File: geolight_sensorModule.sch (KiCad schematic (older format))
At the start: 20 parts, among them IC1 ATTINY841-SSU, P1 5V, P2 ICSP, P3 IN, P4 OUT, P5 OUT (JP for IN), P6 UART(test), U1 TCRT5000/L, Y1 16Mhz

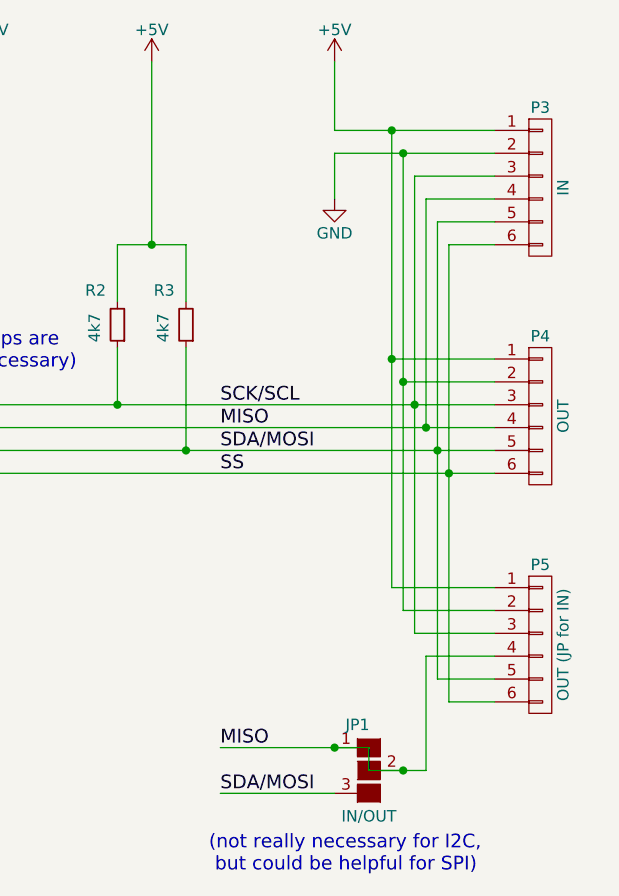
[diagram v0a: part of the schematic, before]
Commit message: removed 3rd, reversible jumper connector (difficult to mirror if reversible, probably not necessary to have 3)
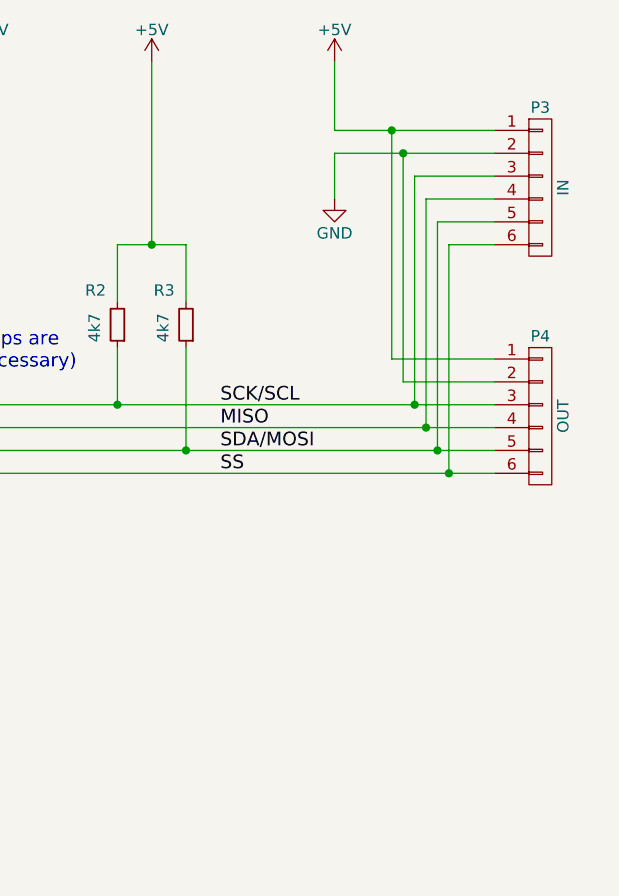
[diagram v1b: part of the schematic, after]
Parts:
- removed JP1: IN/OUT, Connect:GS3, symbol GS3
- removed P5: OUT (JP for IN), Pin_Headers:Pin_Header_Angled_1x06, symbol CONN_01X06
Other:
- note removed: "(not really necessary for I2C, \n but could be helpful for SPI)"
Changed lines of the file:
@@
-$EndComp
-$Comp
-L CONN_01X06 P5
-U 1 1 57CBE4B3
-P 9550 4850
-F 0 "P5" H 9550 5200 50  0000 C CNN
-F 1 "OUT (JP for IN)" V 9650 4850 50  0000 C CNN
-F 2 "Pin_Headers:Pin_Header_Angled_1x06" H 9550 4850 50  0001 C CNN
-F 3 "" H 9550 4850 50  0000 C CNN
-	1    9550 4850
-	1    0    0    -1
 $EndComp
 $Comp
@@
 Text Label 8150 4100 0    60   ~ 0
 SS
-Text Label 8150 5300 0    60   ~ 0
-MISO
-Text Label 8150 5500 0    60   ~ 0
-SDA/MOSI
-$Comp
-L GS3 JP1
-U 1 1 57CC0AD0
-P 8800 5400
-F 0 "JP1" H 8750 5600 50  0000 C CNN
-F 1 "IN/OUT" H 8800 5200 50  0000 C CNN
-F 2 "Connect:GS3" V 8888 5326 50  0001 C CNN
-F 3 "" H 8800 5400 50  0000 C CNN
-	1    8800 5400
-	1    0    0    -1
-$EndComp
 $Comp
 L CONN_02X03 P2
@@
 	1    0    0    -1
 $EndComp
-Wire Wire Line
-	5250 4000 9350 4000
-Wire Wire Line
-	5250 3900 9350 3900
-Connection ~ 6300 2900
-Wire Wire Line
-	5850 2900 6750 2900
-Wire Wire Line
-	9100 5000 9350 5000
-Wire Wire Line
-	9100 3000 9100 5000
-Connection ~ 8900 2600
-Connection ~ 8900 3600
-Wire Wire Line
-	8900 3600 9350 3600
-Connection ~ 8950 3700
-Wire Wire Line
-	9350 3700 8950 3700
-Connection ~ 9000 3800
-Wire Wire Line
-	5250 3800 9350 3800
-Connection ~ 9050 3900
-Connection ~ 9100 4000
-Connection ~ 9150 4100
-Wire Wire Line
-	5250 4100 9350 4100
-Wire Wire Line
-	8900 4600 9350 4600
-Wire Wire Line
-	8650 2600 9350 2600
-Wire Wire Line
-	8900 2600 8900 4600
-Wire Wire Line
-	8950 4700 9350 4700
-Wire Wire Line
-	8650 2700 9350 2700
-Wire Wire Line
-	9000 4800 9350 4800
-Wire Wire Line
-	9000 2800 9000 4800
-Wire Wire Line
-	9350 2800 9000 2800
-Wire Wire Line
-	8800 5400 9050 5400
-Wire Wire Line
-	9350 2900 9050 2900
-Wire Wire Line
-	9100 3000 9350 3000
-Wire Wire Line
-	9150 5100 9350 5100
-Wire Wire Line
-	9150 3100 9150 5100
-Wire Wire Line
-	9350 3100 9150 3100
-Wire Wire Line
-	4300 2700 4300 2800
-Wire Wire Line
-	4300 2400 4300 2500
-Wire Wire Line
-	7150 2350 7150 2300
-Wire Wire Line
-	7000 2350 7150 2350
-Wire Wire Line
-	6700 2350 6800 2350
-Wire Wire Line
-	6750 2900 6750 2650
-Wire Wire Line
-	6750 2650 6700 2650
-Wire Wire Line
-	5850 2650 5850 2900
-Wire Wire Line
-	5900 2650 5850 2650
-Wire Wire Line
-	2500 4400 2500 4850
-Wire Wire Line
-	2750 4400 2500 4400
-Wire Wire Line
-	3150 4500 3000 4500
-Wire Wire Line
-	3150 4300 3000 4300
-Wire Wire Line
-	3450 2700 3450 2650
-Wire Wire Line
-	3650 2700 3450 2700
-Wire Wire Line
-	3450 2500 3450 2550
-Wire Wire Line
-	3650 2500 3450 2500
-Wire Wire Line
-	3650 2700 3650 2900
-Wire Wire Line
-	3650 2300 3650 2500
-Wire Wire Line
-	6250 4600 6250 4850
-Wire Wire Line
-	6100 4600 6250 4600
-Wire Wire Line
-	5700 4600 5900 4600
-Wire Wire Line
-	5250 4600 5500 4600
-Wire Wire Line
-	3150 4600 3100 4600
-Wire Wire Line
-	3100 4600 3100 4750
-Wire Wire Line
-	3050 3400 3150 3400
-Wire Wire Line
-	5250 3400 5700 3400
-Wire Wire Line
-	8150 5300 8800 5300
-Wire Wire Line
-	8650 5500 8150 5500
-Wire Wire Line
-	8800 5300 8800 5400
-Connection ~ 8950 5400
-Connection ~ 8650 5300
-Wire Wire Line
-	9050 2900 9050 3900
-Wire Wire Line
-	8950 2700 8950 4700
-Wire Wire Line
-	8650 2900 8650 2700
-Connection ~ 8950 2700
-Wire Wire Line
-	8650 2600 8650 2300
-Wire Wire Line
-	9350 4900 9050 4900
-Wire Wire Line
-	9050 4900 9050 5400
-Wire Wire Line
-	2050 2650 2650 2650
-Wire Wire Line
-	1550 2550 1050 2550
-Wire Wire Line
-	1550 2650 1050 2650
-Wire Wire Line
-	1550 2750 1050 2750
-Wire Wire Line
-	2050 2750 2150 2750
-Wire Wire Line
-	2150 2750 2150 2900
-Wire Wire Line
-	2050 2550 2150 2550
-Wire Wire Line
-	2150 2550 2150 2300
-Wire Wire Line
-	3150 4200 3050 4200
-Wire Wire Line
-	3050 4200 3050 3900
-Wire Wire Line
-	3050 2300 3050 3700
-Connection ~ 3050 3400
-Wire Wire Line
-	4700 2800 4700 2700
-Wire Wire Line
-	4700 2400 4700 2500
-Wire Wire Line
-	4300 2800 4700 2800
-Wire Wire Line
-	4500 2900 4500 2800
-Connection ~ 4500 2800
 $Comp
 L +5V #PWR013
@@
 	1    0    0    -1
 $EndComp
-Wire Wire Line
-	4300 2400 4700 2400
-Wire Wire Line
-	4500 2300 4500 2400
-Connection ~ 4500 2400
-Wire Wire Line
-	3100 4750 2500 4750
-Connection ~ 2500 4750
 $Comp
 L R_Small R2
@@
 	-1   0    0    1
 $EndComp
-Wire Wire Line
-	7700 3550 7700 3800
-Wire Wire Line
-	8000 3550 8000 4000
-Wire Wire Line
-	5700 3400 5700 2350
-Wire Wire Line
-	7700 3350 7700 3100
-Wire Wire Line
-	8000 3100 8000 3350
 $Comp
 L +5V #PWR014
@@
 	1    0    0    -1
 $EndComp
-Connection ~ 7850 3100
 Text Notes 6700 3650 0    60   ~ 0
 (these pullups are \n likely unnecessary)
-Wire Wire Line
-	5250 3500 5450 3500
-Wire Wire Line
-	5250 3600 5450 3600
-Wire Wire Line
-	7700 3100 8000 3100
-Wire Wire Line
-	7850 2300 7850 3100
-Wire Wire Line
-	5550 2350 5900 2350
-Connection ~ 7700 3800
-Connection ~ 8000 4000
-Text Notes 8100 5850 0    60   ~ 0
-(not really necessary for I2C, \n but could be helpful for SPI)
 $Comp
 L CONN_01X02 P6
@@
 $EndComp
 Wire Wire Line
+	5250 4000 9350 4000
+Wire Wire Line
+	5250 3900 9350 3900
+Connection ~ 6300 2900
+Wire Wire Line
+	5850 2900 6750 2900
+Connection ~ 8900 2600
+Wire Wire Line
+	8900 3600 9350 3600
+Wire Wire Line
+	9350 3700 8950 3700
+Connection ~ 9000 3800
+Wire Wire Line
+	5250 3800 9350 3800
+Connection ~ 9050 3900
+Connection ~ 9100 4000
+Connection ~ 9150 4100
+Wire Wire Line
+	5250 4100 9350 4100
+Wire Wire Line
+	8650 2600 9350 2600
+Wire Wire Line
+	8650 2700 9350 2700
+Wire Wire Line
+	9350 2800 9000 2800
+Wire Wire Line
+	9350 2900 9050 2900
+Wire Wire Line
+	9100 3000 9350 3000
+Wire Wire Line
+	9350 3100 9150 3100
+Wire Wire Line
+	4300 2700 4300 2800
+Wire Wire Line
+	4300 2400 4300 2500
+Wire Wire Line
+	7150 2350 7150 2300
+Wire Wire Line
+	7000 2350 7150 2350
+Wire Wire Line
+	6700 2350 6800 2350
+Wire Wire Line
+	6750 2900 6750 2650
+Wire Wire Line
+	6750 2650 6700 2650
+Wire Wire Line
+	5850 2650 5850 2900
+Wire Wire Line
+	5900 2650 5850 2650
+Wire Wire Line
+	2500 4400 2500 4850
+Wire Wire Line
+	2750 4400 2500 4400
+Wire Wire Line
+	3150 4500 3000 4500
+Wire Wire Line
+	3150 4300 3000 4300
+Wire Wire Line
+	3450 2700 3450 2650
+Wire Wire Line
+	3650 2700 3450 2700
+Wire Wire Line
+	3450 2500 3450 2550
+Wire Wire Line
+	3650 2500 3450 2500
+Wire Wire Line
+	3650 2700 3650 2900
+Wire Wire Line
+	3650 2300 3650 2500
+Wire Wire Line
+	6250 4600 6250 4850
+Wire Wire Line
+	6100 4600 6250 4600
+Wire Wire Line
+	5700 4600 5900 4600
+Wire Wire Line
+	5250 4600 5500 4600
+Wire Wire Line
+	3150 4600 3100 4600
+Wire Wire Line
+	3100 4600 3100 4750
+Wire Wire Line
+	3050 3400 3150 3400
+Wire Wire Line
+	5250 3400 5700 3400
+Wire Wire Line
+	9050 2900 9050 3900
+Wire Wire Line
+	8650 2900 8650 2700
+Connection ~ 8950 2700
+Wire Wire Line
+	8650 2600 8650 2300
+Wire Wire Line
+	2050 2650 2650 2650
+Wire Wire Line
+	1550 2550 1050 2550
+Wire Wire Line
+	1550 2650 1050 2650
+Wire Wire Line
+	1550 2750 1050 2750
+Wire Wire Line
+	2050 2750 2150 2750
+Wire Wire Line
+	2150 2750 2150 2900
+Wire Wire Line
+	2050 2550 2150 2550
+Wire Wire Line
+	2150 2550 2150 2300
+Wire Wire Line
+	3150 4200 3050 4200
+Wire Wire Line
+	3050 4200 3050 3900
+Wire Wire Line
+	3050 2300 3050 3700
+Connection ~ 3050 3400
+Wire Wire Line
+	4700 2800 4700 2700
+Wire Wire Line
+	4700 2400 4700 2500
+Wire Wire Line
+	4300 2800 4700 2800
+Wire Wire Line
+	4500 2900 4500 2800
+Connection ~ 4500 2800
+Wire Wire Line
+	4300 2400 4700 2400
+Wire Wire Line
+	4500 2300 4500 2400
+Connection ~ 4500 2400
+Wire Wire Line
+	3100 4750 2500 4750
+Connection ~ 2500 4750
+Wire Wire Line
+	7700 3550 7700 3800
+Wire Wire Line
+	8000 3550 8000 4000
+Wire Wire Line
+	5700 3400 5700 2350
+Wire Wire Line
+	7700 3350 7700 3100
+Wire Wire Line
+	8000 3100 8000 3350
+Connection ~ 7850 3100
+Wire Wire Line
+	5250 3500 5450 3500
+Wire Wire Line
+	5250 3600 5450 3600
+Wire Wire Line
+	7700 3100 8000 3100
+Wire Wire Line
+	7850 2300 7850 3100
+Wire Wire Line
+	5550 2350 5900 2350
+Connection ~ 7700 3800
+Connection ~ 8000 4000
+Wire Wire Line
 	5200 2300 5200 2350
 Wire Wire Line
 	5200 2350 5350 2350
 Connection ~ 5700 2350
+Wire Wire Line
+	9150 3100 9150 4100
+Wire Wire Line
+	9100 3000 9100 4000
+Wire Wire Line
+	9000 2800 9000 3800
+Wire Wire Line
+	8950 3700 8950 2700
+Wire Wire Line
+	8900 2600 8900 3600
 $EndSCHEMATC

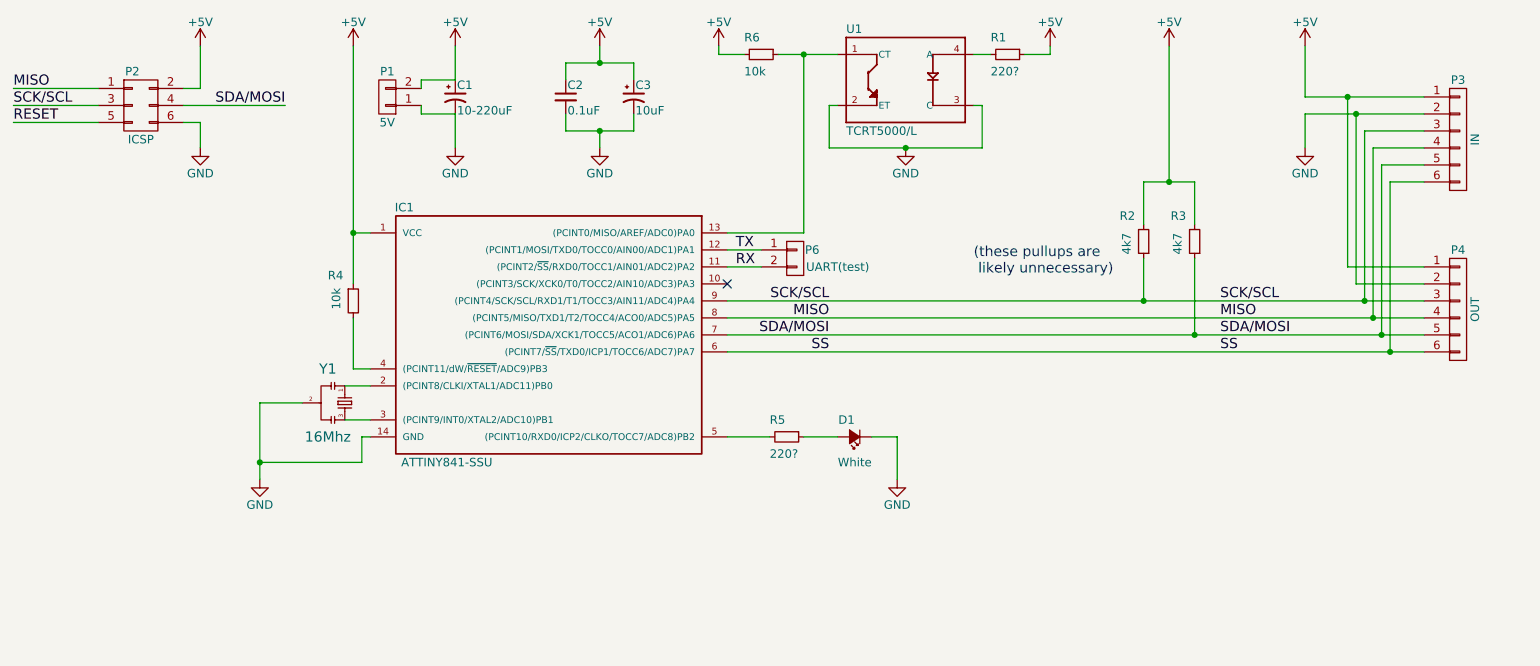
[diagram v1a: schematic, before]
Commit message: clean up schematic. Add SPI/I2C jumper.
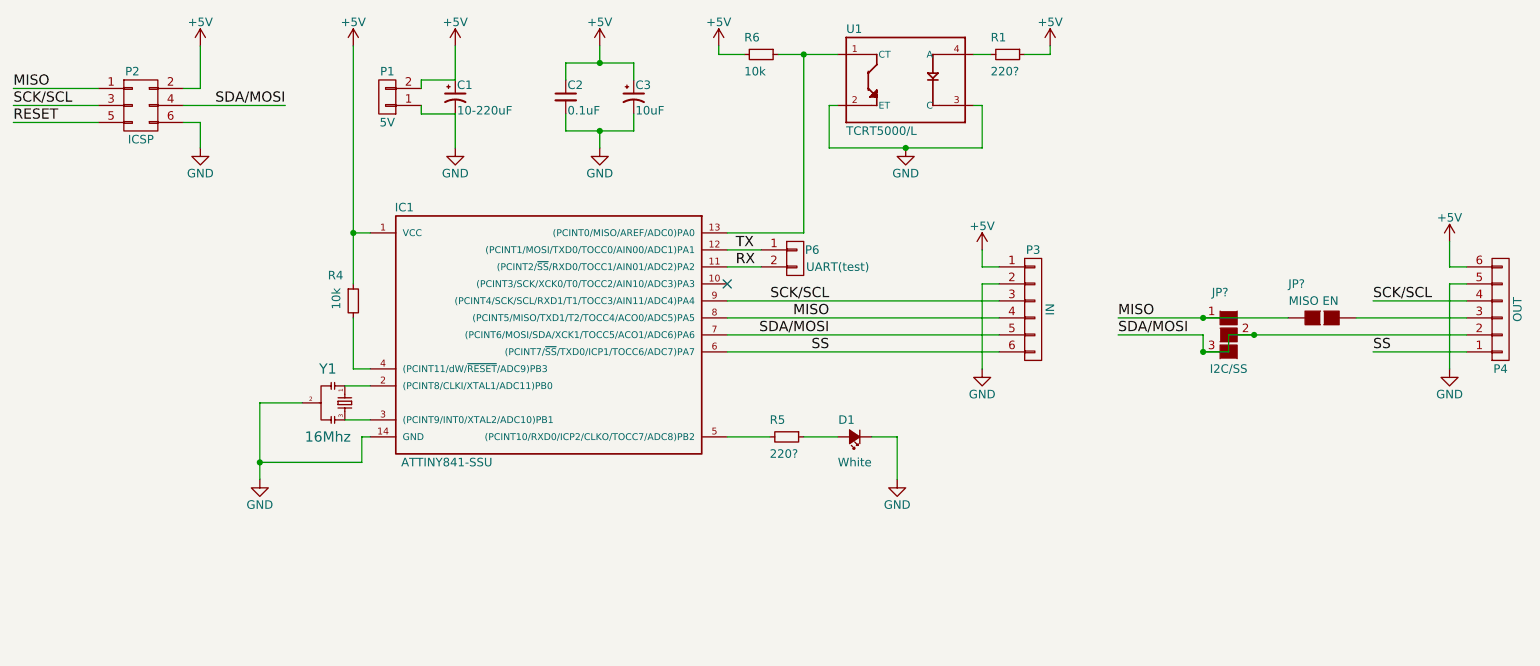
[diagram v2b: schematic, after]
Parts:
- removed R2, R3: 4k7, Discret:R1, symbol R_Small
- added JP?: I2C/SS, GS3, symbol GS3
- added JP?: MISO EN, GS2, symbol GS2
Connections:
- net +5V: now also P4.6 (P6); no longer P4.1 (P1)
- net GND: now also P4.5 (P5); no longer P4.2 (P2)
- net MISO: now also JP?.1 (G1), JP?.2 (G2); no longer P4.4 (P4)
- net SCK/SCL: now also P4.4 (P4); no longer P4.3 (P3)
- net SDA/MOSI: now also P4.2 (P2), JP?.2 (G2), JP?.3 (G3); no longer P4.5 (P5)
- net SS: now also P4.1 (P1); no longer P4.6 (P6)
- new net: JP?.1 (G1), P4.3 (P3)
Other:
- note removed: "(these pullups are \n likely unnecessary)"
- moved on the sheet: P3, P4

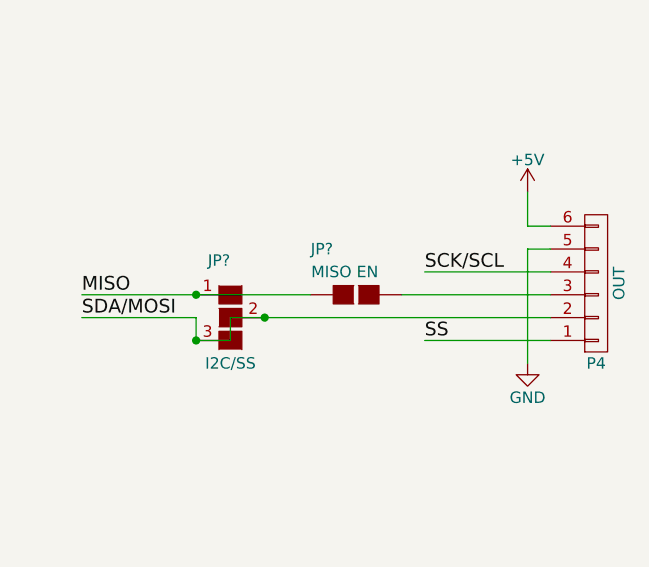
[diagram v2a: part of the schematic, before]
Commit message: fixed mirrored in/out. updated netlist, footprints, PCB. Fixed UART test point rats nest
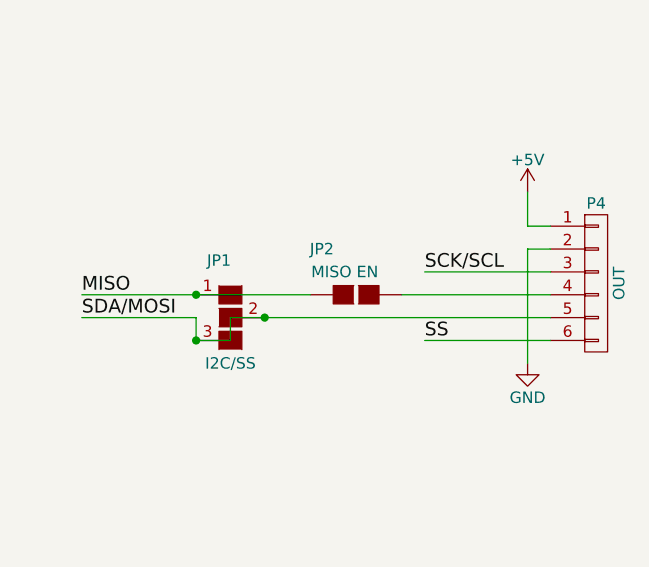
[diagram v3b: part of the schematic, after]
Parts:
- JP1: renamed from JP?; footprint GS3 -> Connect:GS3
- JP2: renamed from JP?; footprint GS2 -> Connect:GS2
- P3, P4: footprint Pin_Headers:Pin_Header_Angled_1x06 -> Pin_Headers:Pin_Header_Straight_1x06
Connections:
- net +5V: now also P4.1 (P1); no longer P4.6 (P6)
- net GND: now also P4.2 (P2); no longer P4.5 (P5)
- net SCK/SCL: now also P4.3 (P3); no longer P4.4 (P4)
- net SDA/MOSI: now also P4.5 (P5); no longer P4.2 (P2)
- net SS: now also P4.6 (P6); no longer P4.1 (P1)
- net at JP2.1 (G1): now also P4.4 (P4); no longer P4.3 (P3)
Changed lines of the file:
@@
 F 0 "P3" H 7050 4200 50  0000 C CNN
 F 1 "IN" V 7150 3850 50  0000 C CNN
-F 2 "Pin_Headers:Pin_Header_Angled_1x06" H 7050 3850 50  0001 C CNN
+F 2 "Pin_Headers:Pin_Header_Straight_1x06" H 7050 3850 50  0001 C CNN
 F 3 "" H 7050 3850 50  0000 C CNN
 	1    7050 3850
@@
 F 0 "P4" H 9800 4200 50  0000 C CNN
 F 1 "OUT" V 9900 3850 50  0000 C CNN
-F 2 "Pin_Headers:Pin_Header_Angled_1x06" H 9800 3850 50  0001 C CNN
+F 2 "Pin_Headers:Pin_Header_Straight_1x06" H 9800 3850 50  0001 C CNN
 F 3 "" H 9800 3850 50  0000 C CNN
 	1    9800 3850
-	1    0    0    1
+	1    0    0    -1
 $EndComp
 $Comp
@@
 SDA/MOSI
 $Comp
-L GND #PWR010
+L GND #PWR09
 U 1 1 57CC2E31
 P 2150 2900
-F 0 "#PWR010" H 2150 2650 50  0001 C CNN
+F 0 "#PWR09" H 2150 2650 50  0001 C CNN
 F 1 "GND" H 2150 2750 50  0000 C CNN
 F 2 "" H 2150 2900 50  0000 C CNN
@@
 $EndComp
 $Comp
-L +5V #PWR011
+L +5V #PWR010
 U 1 1 57CC2EE1
 P 2150 2300
-F 0 "#PWR011" H 2150 2150 50  0001 C CNN
+F 0 "#PWR010" H 2150 2150 50  0001 C CNN
 F 1 "+5V" H 2150 2440 50  0000 C CNN
 F 2 "" H 2150 2300 50  0000 C CNN
@@
 $EndComp
 $Comp
-L GND #PWR012
+L GND #PWR011
 U 1 1 57CC3ABE
 P 4500 2900
-F 0 "#PWR012" H 4500 2650 50  0001 C CNN
+F 0 "#PWR011" H 4500 2650 50  0001 C CNN
 F 1 "GND" H 4500 2750 50  0000 C CNN
 F 2 "" H 4500 2900 50  0000 C CNN
@@
 $EndComp
 $Comp
-L +5V #PWR013
+L +5V #PWR012
 U 1 1 57CC3AB8
 P 4500 2300
-F 0 "#PWR013" H 4500 2150 50  0001 C CNN
+F 0 "#PWR012" H 4500 2150 50  0001 C CNN
 F 1 "+5V" H 4500 2440 50  0000 C CNN
 F 2 "" H 4500 2300 50  0000 C CNN
@@
 $EndComp
 $Comp
-L +5V #PWR015
+L +5V #PWR013
 U 1 1 57CBD563
 P 5200 2300
-F 0 "#PWR015" H 5200 2150 50  0001 C CNN
+F 0 "#PWR013" H 5200 2150 50  0001 C CNN
 F 1 "+5V" H 5200 2440 50  0000 C CNN
 F 2 "" H 5200 2300 50  0000 C CNN
@@
 $EndComp
 $Comp
-L +5V #PWR?
+L +5V #PWR014
 U 1 1 57CBF61D
 P 9500 3450
-F 0 "#PWR?" H 9500 3300 50  0001 C CNN
+F 0 "#PWR014" H 9500 3300 50  0001 C CNN
 F 1 "+5V" H 9500 3590 50  0000 C CNN
 F 2 "" H 9500 3450 50  0000 C CNN
@@
 $EndComp
 $Comp
-L GND #PWR?
+L GND #PWR015
 U 1 1 57CBF758
 P 9500 4200
-F 0 "#PWR?" H 9500 3950 50  0001 C CNN
+F 0 "#PWR015" H 9500 3950 50  0001 C CNN
 F 1 "GND" H 9500 4050 50  0000 C CNN
 F 2 "" H 9500 4200 50  0000 C CNN
@@
 	8050 4100 8200 4100
 $Comp
-L GS3 JP?
+L GS3 JP1
 U 1 1 57CC065C
 P 8200 4000
-F 0 "JP?" H 8150 4250 50  0000 C CNN
+F 0 "JP1" H 8150 4250 50  0000 C CNN
 F 1 "I2C/SS" H 8200 3800 50  0000 C CNN
-F 2 "GS3" V 8288 3926 50  0001 C CNN
+F 2 "Connect:GS3" V 8288 3926 50  0001 C CNN
 F 3 "" H 8200 4000 50  0000 C CNN
 	1    8200 4000
@@
 	6750 3600 6850 3600
 $Comp
-L GND #PWR?
+L GND #PWR016
 U 1 1 57CC13DF
 P 6750 4200
-F 0 "#PWR?" H 6750 3950 50  0001 C CNN
+F 0 "#PWR016" H 6750 3950 50  0001 C CNN
 F 1 "GND" H 6750 4050 50  0000 C CNN
 F 2 "" H 6750 4200 50  0000 C CNN
@@
 	9500 3600 9600 3600
 $Comp
-L GS2 JP?
+L GS2 JP2
 U 1 1 57CC1D1D
 P 8750 3900
-F 0 "JP?" V 8550 3750 50  0000 C CNN
+F 0 "JP2" V 8550 3750 50  0000 C CNN
 F 1 "MISO EN" V 8650 3850 50  0000 C CNN
-F 2 "GS2" V 8824 3900 50  0001 C CNN
+F 2 "Connect:GS2" V 8824 3900 50  0001 C CNN
 F 3 "" H 8750 3900 50  0000 C CNN
 	1    8750 3900

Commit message: minor changes.
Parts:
- added P5: AUX_SENSOR, Pin_Headers:Pin_Header_Straight_1x03, symbol CONN_01X03
- P6: value UART(test) -> UART
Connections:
- net +5V: now also P5.1 (P1)
- net GND: now also P5.3 (P3)
- net AUX: now reaches IC1.10 ((PCINT3/SCK/XCK0/T0/TOCC2/AIN10/ADC3)PA3)
- net AUX: now also P5.2 (P2)
- no-connect marks 1 -> 0
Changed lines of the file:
@@
 	0    -1   -1   0
 $EndComp
-NoConn ~ 5250 3700
 $Comp
 L TCRT5000L U1
@@
 P 5650 3550
 F 0 "P6" H 5750 3600 50  0000 C CNN
-F 1 "UART(test)" H 5900 3500 50  0000 C CNN
+F 1 "UART" H 5800 3500 50  0000 C CNN
 F 2 "Measurement_Points:Test_Point" H 5650 3550 50  0001 C CNN
 F 3 "" H 5650 3550 50  0000 C CNN
@@
 Wire Wire Line
 	8050 4000 8050 4100
+Text Label 5450 3700 2    60   ~ 0
+AUX
+Wire Wire Line
+	5250 3700 5450 3700
+$Comp
+L CONN_01X03 P5
+U 1 1 57CE756D
+P 9800 2550
+F 0 "P5" H 9800 2750 50  0000 C CNN
+F 1 "AUX_SENSOR" V 9900 2550 50  0000 C CNN
+F 2 "Pin_Headers:Pin_Header_Straight_1x03" H 9800 2550 50  0001 C CNN
+F 3 "" H 9800 2550 50  0000 C CNN
+	1    9800 2550
+	1    0    0    -1
+$EndComp
+Text Label 9350 2550 0    60   ~ 0
+AUX
+Wire Wire Line
+	9600 2550 9350 2550
+$Comp
+L +5V #PWR017
+U 1 1 57CE76AC
+P 9500 2300
+F 0 "#PWR017" H 9500 2150 50  0001 C CNN
+F 1 "+5V" H 9500 2440 50  0000 C CNN
+F 2 "" H 9500 2300 50  0000 C CNN
+F 3 "" H 9500 2300 50  0000 C CNN
+	1    9500 2300
+	1    0    0    -1
+$EndComp
+Wire Wire Line
+	9500 2300 9500 2450
+Wire Wire Line
+	9500 2450 9600 2450
+$Comp
+L GND #PWR018
+U 1 1 57CE7889
+P 9500 2900
+F 0 "#PWR018" H 9500 2650 50  0001 C CNN
+F 1 "GND" H 9500 2750 50  0000 C CNN
+F 2 "" H 9500 2900 50  0000 C CNN
+F 3 "" H 9500 2900 50  0000 C CNN
+	1    9500 2900
+	1    0    0    -1
+$EndComp
+Wire Wire Line
+	9600 2650 9500 2650
+Wire Wire Line
+	9500 2650 9500 2900
 $EndSCHEMATC
